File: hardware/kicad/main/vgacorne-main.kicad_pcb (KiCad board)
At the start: 2 copper layers, 154.9 x 105.9 mm, 162 parts, among them J1 TYPE-C-31-M-12, J2 SWD, J3 SM10B-SRSS-TB, J4 MCU module, J5 Trackpad, SW1 C0R0, SW10 C3R0, SW11 C3R1, SW12 C3R2, SW13 C4R0, SW14 C4R1, SW15 C4R2, SW16 C5R0, SW17 C5R1, SW18 C5R2, SW19 T0, SW2 C0R1, SW20 T1, SW21 T2, SW22 BOOT, SW23 RESET, SW3 C0R2, SW4 C1R0, SW5 C1R1, SW6 C1R2, SW7 C2R0, SW8 C2R1, SW9 C2R2, U11 SN74LV4051APWR, U12 SN74LV4051APWR, U13 SN74LV4051APWR, U2 TLV75733PDBVR, U3 TLV75733PDBVR, U4 USBLC6-2SC6, U6 SRV05-4, U7 SRV05-4, U8 TPS2051CDBVR

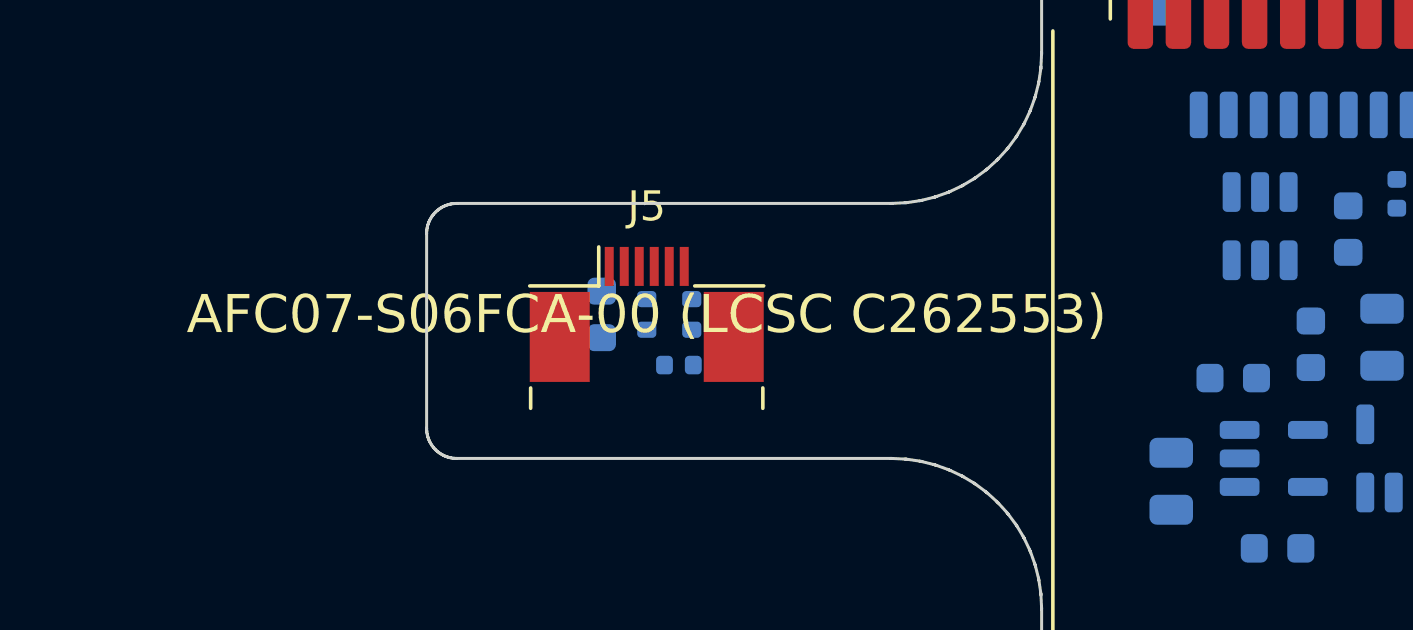
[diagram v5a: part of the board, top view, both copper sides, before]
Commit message: Make the MCU modules 4-layer and route them
The modules are now 1.0 mm 4-layer boards with a solid GND plane on In1
and +3V3 on In2, so every cap and supply pin drops a via and the signals,
USB included, run over unbroken ground. Their support parts are placed
beside the LQFP pins they serve (each 100 nF at its supply pin, the
crystal at the oscillator pins). Module net classes: 0.15 mm clearance,
USB 0.2/0.15 mm (~91 ohm over the plane on JLC's 1.0 mm stack-up).
Castellated pads connect solidly to the planes.

route.py learns to route to castellated edge pads (routing area grown
past the edge, keepouts holding the copper-to-edge clearance), to fan
plane-net pads out to their own vias before routing, and to fall back to
one-pass routing on 2-layer boards. Both modules route completely and
pass DRC.

Also: part-number and tolerance fields no longer print on the
silkscreen.

Co-Authored-By: Claude Opus 5.5 (1M context) <noreply@anthropic.com>
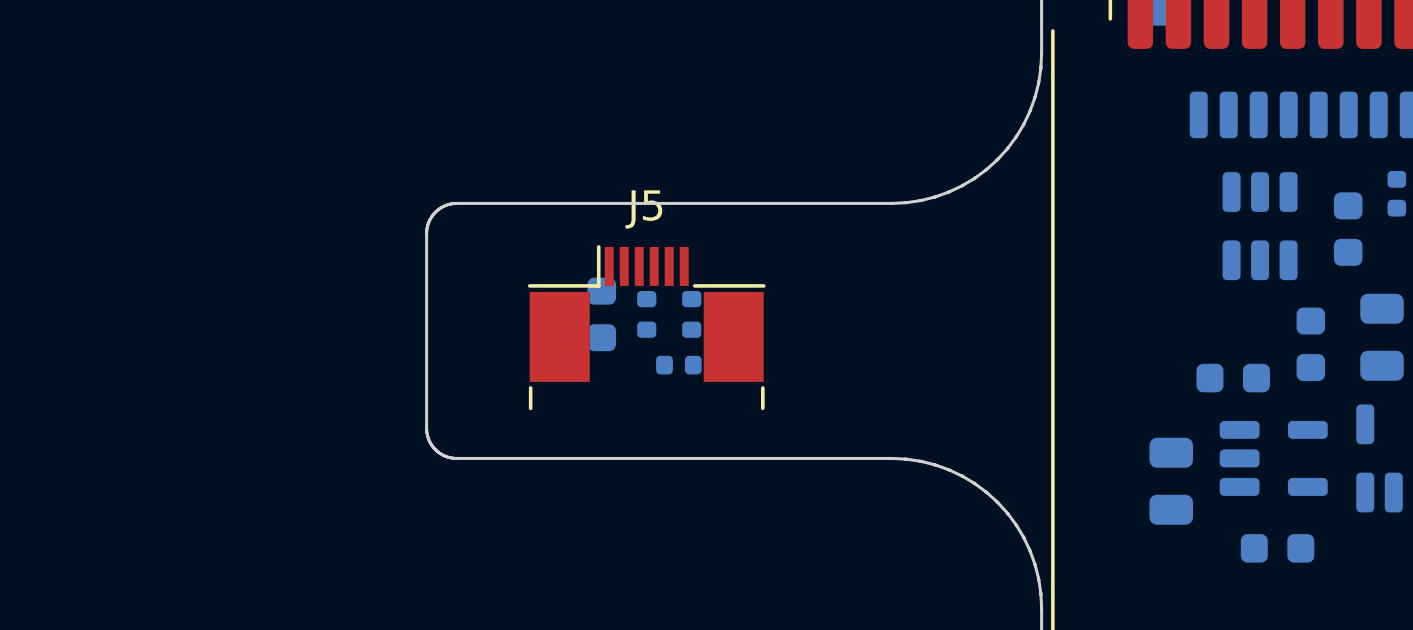
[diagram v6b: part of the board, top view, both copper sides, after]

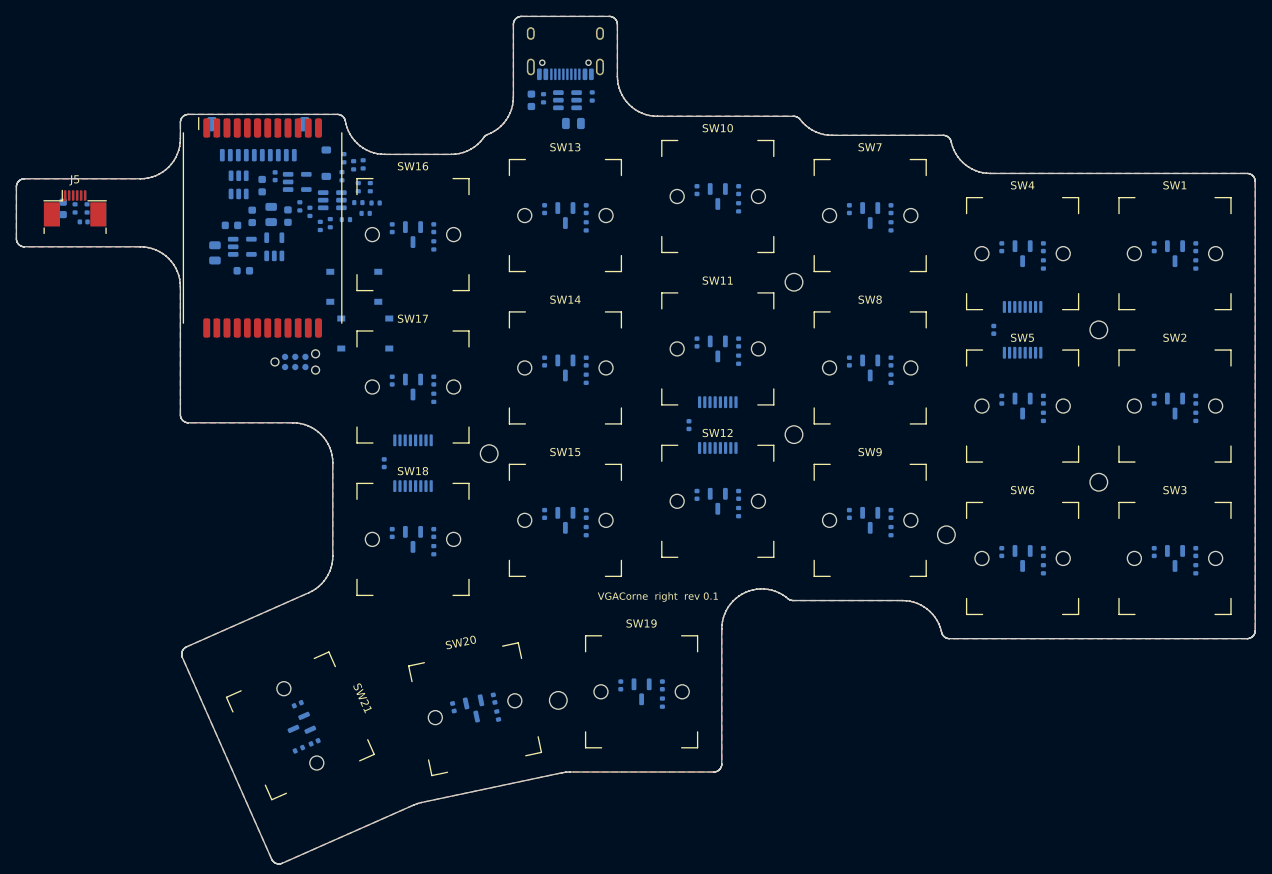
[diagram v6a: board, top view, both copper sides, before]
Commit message: Route the satellite and most of the main board
route.py now runs its strategies in parallel and keeps the first that
connects everything, streams Freerouting's logs to route-logs/, drops stray
vias, adds a finishing pass on boards left with gaps, and stitches ground
every 5 mm on large boards (2.5 mm on small ones).

The satellite is fully routed. On the main board the regulators moved to
the USB-C ear and the remote ADC resistors to the module's ADC pads, which
took the unconnected count from 9 to 3. The Power class is 0.3 mm so
tracks can enter 0.5 mm-pitch pads.

The main board is not finished: LINK_B (J3.7-U7.3), VBUS at USB-C A4 and
LINK_A at R8.1 are still open, C18's ground pad has no via to the pour
(starved thermal, so `generate.py check` fails), and the USB pair needs
rerouting as a coupled pair. docs/bring-up.md lists the steps.

Co-Authored-By: Claude Opus 5.5 (1M context) <noreply@anthropic.com>
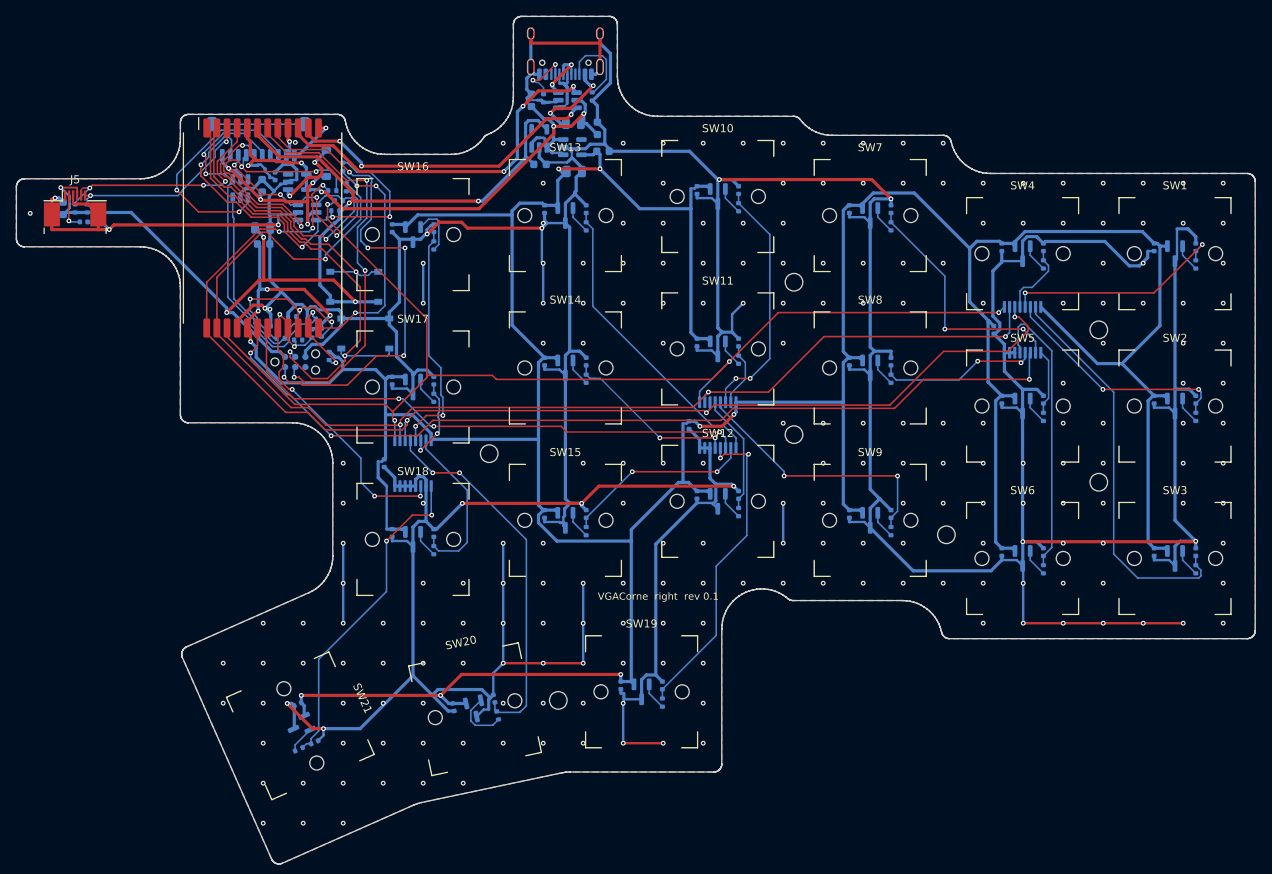
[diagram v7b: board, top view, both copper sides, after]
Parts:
- moved C2 47.7 mm to (206.4, 37.2), turned to 90 degrees
- moved C3 47.4 mm to (207.1, 40.1)
- moved C4 46.1 mm to (203.5, 42.6), turned to 0 degrees
- moved U2 43.1 mm to (203.3, 39.5)
- moved C5 36.6 mm to (199.2, 41.7), turned to 0 degrees
- moved U3 35.8 mm to (199.1, 38.5)
- moved R9 23.9 mm to (166.8, 63.4), turned to 180 degrees
- moved R10 21.8 mm to (168.4, 62.2), turned to 180 degrees
- moved R14 21.1 mm to (166.1, 61.9), turned to 180 degrees
- moved R16 20.4 mm to (170.7, 61.0), turned to 180 degrees
- moved R13 19.1 mm to (172.9, 65.6), turned to 90 degrees
- moved R8 16.1 mm to (169.0, 63.6), turned to 180 degrees
- moved R11 14.9 mm to (170.7, 62.8), turned to 90 degrees
- moved R12 13.7 mm to (171.9, 62.7), turned to 90 degrees
- moved R15 11.9 mm to (168.2, 60.7), turned to 180 degrees
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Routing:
- net GND: track 0.00 -> 901.5 mm, vias 0 -> 232
- net +3.3VA: track 0.00 -> 533.6 mm, vias 0 -> 11
- net /MUX_S1: track 0.00 -> 152.0 mm, vias 0 -> 4
- net /MUX_S0: track 0.00 -> 151.2 mm, vias 0 -> 6
- net /MUX_S2: track 0.00 -> 146.1 mm, vias 0 -> 4
- net +3V3: track 0.00 -> 140.6 mm, vias 0 -> 6
- net /ADC_L_A: track 0.00 -> 111.8 mm, vias 0 -> 3
- net +5V: track 0.00 -> 81.5 mm, vias 0 -> 5
- net /ADC_L_B: track 0.00 -> 67.6 mm, vias 0 -> 3
- net /SWDIO: track 0.00 -> 61.1 mm, vias 0 -> 5
- net /NRST: track 0.00 -> 59.4 mm, vias 0 -> 2
- net /LINK_DET: track 0.00 -> 51.2 mm, vias 0 -> 4
- net /HE_C0R2: track 0.00 -> 49.9 mm
- net /SWCLK: track 0.00 -> 49.4 mm, vias 0 -> 3
- net /HE_T1: track 0.00 -> 46.5 mm, vias 0 -> 2
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
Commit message: Main board fully routed: spread out the link cluster; fix starved pads
- pcb.py: autoplace takes a courtyard gap; LINK_GAP = 1.0 mm (was 0.15) for
  the link and ADC-resistor groups beside the module. 20 small bottom-side
  parts move 1-10 mm; connectors, module, switches and bosses stay put.
- Re-routed with route.py (Freerouting 2.4.1): 0 unconnected, against 3
  before. Of 0.5/0.8/1.0/1.2/1.5 mm gaps, 1.0 mm routed cleanest.
- route.py: fix_starved() gives any ground pad DRC finds short of thermal
  spokes a solid connection and a via of its own (R15 here; C18 before).
  fanout() can now place vias around existing tracks.
- generate.py check passes on every board for the first time; the 3D case
  is unchanged, the right case foam follows the moved parts.
- Only the USB pair is left to route as a differential pair in KiCad.
  Freerouting 2.5.0 and Quilter were tried first and didn't beat this.

Co-Authored-By: Claude Opus 5.5 <noreply@anthropic.com>
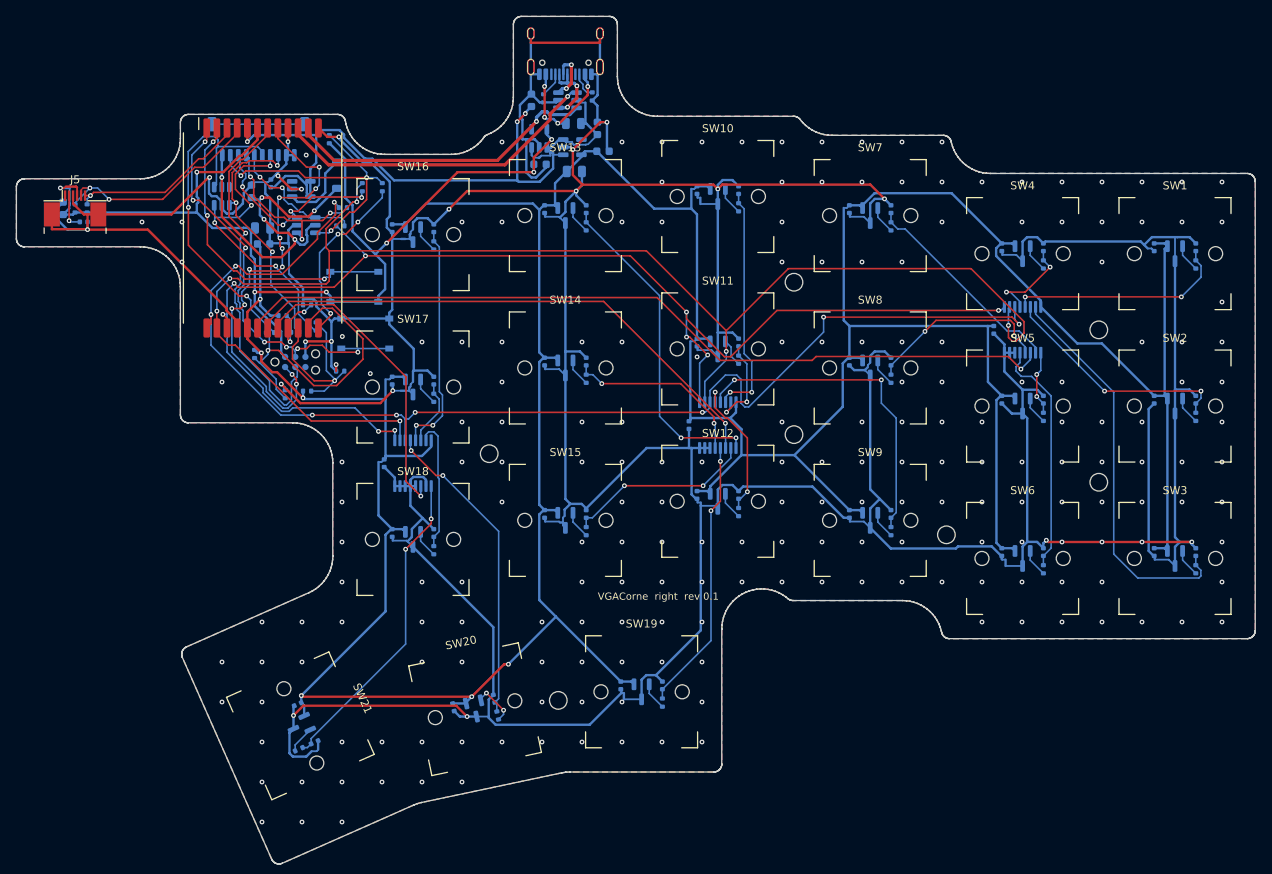
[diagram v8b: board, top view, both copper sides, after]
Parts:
- moved R16 9.97 mm to (167.4, 70.4), turned to 90 degrees
- moved R13 9.33 mm to (163.5, 65.4)
- moved R15 9.09 mm to (174.2, 67.5)
- moved R17 8.96 mm to (172.9, 38.6), turned to -90 degrees
- moved R12 7.53 mm to (170.1, 70.0), turned to 180 degrees
- moved R18 5.55 mm to (179.5, 44.5)
- moved R14 4.83 mm to (170.1, 59.3)
- moved R9 4.66 mm to (171.2, 62.0), turned to 90 degrees
- moved R11 4.31 mm to (167.0, 60.6), turned to 180 degrees
- moved R7 3.16 mm to (174.3, 49.4)
- moved R10 2.92 mm to (165.5, 62.7)
- moved U7 2.51 mm to (159.4, 45.7)
- moved R5 2.50 mm to (174.6, 47.1)
- moved R6 2.00 mm to (177.0, 44.5)
- moved D1 1.99 mm to (173.8, 43.0)
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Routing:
- net GND: track 901.5 -> 850.3 mm, vias 232 -> 225
- net /MUX_S1: track 152.0 -> 179.6 mm, vias 4 -> 6
- net /ADC_R_C: track 13.8 -> 38.6 mm, vias 2 -> 1
- net +3.3VA: track 533.6 -> 512.9 mm, vias 11 -> 6
- net /+5V_LINK: track 26.6 -> 47.1 mm, vias 4 -> 5
- net /LINK_S2: track 36.3 -> 17.2 mm
- net /MUX_S2: track 146.1 -> 163.2 mm, vias 4 -> 9
- net /LINK_B: track 22.0 -> 38.5 mm, vias 0 -> 4
- net /LINK_DET: track 51.2 -> 39.8 mm, vias 4 -> 3
- net /LINK_S0: track 33.6 -> 22.5 mm
- net +5V: track 81.5 -> 91.7 mm, vias 5 -> 3
- net /HE_C2R2: track 33.4 -> 41.3 mm
- net /DET: track 29.9 -> 22.1 mm
- net /ADC_L_A: track 111.8 -> 104.1 mm, vias 3 -> 1
- net /HE_T1: track 46.5 -> 39.3 mm
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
